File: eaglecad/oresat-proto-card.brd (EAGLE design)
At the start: 99.8 x 94.7 mm, 263 parts, among them J6 J-SAMTEC-TFM-120-X1-XXX-D-RA, Q10 DMP2240UDM, Q11 MOSFET-PCH-SOT23-6, Q12 MOSFET-PCH-SOT23-6, Q13 PMV45EN, Q14 PMV45EN, Q15 DMP2240UDM, Q16 MOSFET-PCH-SOT23-6, Q17 MOSFET-PCH-SOT23-6, Q18 PMV45EN, Q19 PMV45EN, Q20 DMP2240UDM, Q21 MOSFET-PCH-SOT23-6, Q22 MOSFET-PCH-SOT23-6, Q23 PMV45EN, Q24 PMV45EN, Q25 DMP2240UDM, Q6 MOSFET-PCH-SOT23-6, Q7 MOSFET-PCH-SOT23-6, Q8 PMV45EN, Q9 PMV45EN, U10 MAX7310ATE, U11 MAX4211CETE, U12 MCP1703A, U13 MAX7310ATE, U14 MAX4211CETE, U15 MCP1703A, U3 MAX7310ATE, U4 MAX4211CETE, U6 MCP1703A, U7 MAX7310ATE, U8 MAX4211CETE, U9 MCP1703A

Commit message: power domain updates
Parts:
- removed C21, C22: 1u, oresat-rcl:.0603-B-NOSILK
- removed C23, C24: TBD, rcl_custom:.0402-B-NOSILK
- removed C25: 100n, rcl_custom:.0402-B-NOSILK
- removed D10: AMBER, SparkFun-LED:LED-0603
- removed D9: GREEN, SparkFun-LED:LED-0603
- removed Q21, Q22: MOSFET-PCH-SOT23-6, Q-MOSFET-PCH-SOT23-6:SOT23-6
- removed Q23, Q24: PMV45EN, Tova:SOT23
- removed Q25: DMP2240UDM, Q-MOSFET-PCH-dual-SOT23-6:SOT23-6
- removed R153, R154, R163, R165, R167, R168, R38: NP, rcl_custom:.0402-B-NOSILK
- removed R155, R156, R37: 100, rcl_custom:.0402-B-NOSILK
- removed R157, R158, R159, R161, R166, R169, R171, R172, R173: 10k, rcl_custom:.0402-B-NOSILK
- removed R160: 100m, rcl:R1206
- removed R162, R164: 0, rcl_custom:.0402-B-NOSILK
- removed R170, R36: 2.7k, rcl_custom:.0402-B-NOSILK
- removed R174, R175: 47k, rcl_custom:.0402-B-NOSILK
- removed TP13, TP14, TP18, TP20, TP22: TEST-POINT, Tova:2MM-TEST-POINT
- removed U3: MAX7310ATE, U-Maxim-MAX7310-I2C-GPIO-expander:QFN65P400X400X80-17T210
- removed U4: MAX4211CETE, U-Maxim-MAX4211-power-monitor:QFN65P400X400X80-17T210
- added C6: 100n, rcl_custom:.0402-B-NOSILK
- added D11: GREEN, SparkFun-LED:LED-0603
- added D12: AMBER, SparkFun-LED:LED-0603
- added Q26, Q27: MOSFET-PCH-SOT23-6, Q-MOSFET-PCH-SOT23-6:SOT23-6
- added Q28, Q29: PMV45EN, Tova:SOT23
- added Q30: DMP2240UDM, Q-MOSFET-PCH-dual-SOT23-6:SOT23-6
- added R191, R219: 2.7k, rcl_custom:.0402-B-NOSILK
- added R192, R205, R225: 100, rcl_custom:.0402-B-NOSILK
- added R193, R194, R195, R196, R197, R198, R199, R200, R201, R202, R203, R204, R212, R214, R216, R217: NP, rcl_custom:.0402-B-NOSILK
- added R206, R207, R208, R210, R215, R218, R220, R226: 10k, rcl_custom:.0402-B-NOSILK
- added R209: 100m, rcl:R1206
- added R211, R213: 0, rcl_custom:.0402-B-NOSILK
- added R221, R222: 47k, rcl_custom:.0402-B-NOSILK
- added R223, R227: 330k, rcl_custom:.0402-B-NOSILK
- added R224, R228: 1M, rcl_custom:.0402-B-NOSILK
- added TP2, TP4, TP76, TP77, TP78, TP79, TP80, TP81, TP82, TP83, TP84, TP85, TP86, TP87, TP88, TP89, TP90: TEST-POINT, Tova:2MM-TEST-POINT
- added U16, U23, U24: MIC842LYC5, U-Microchip-MIC842-Comparator:SC70-5
- added U21, U5: MAX7310ATE, U-Maxim-MAX7310-I2C-GPIO-expander:QFN65P400X400X80-17T210
- added U22: MAX4211FETE, U-Maxim-MAX4211-power-monitor:QFN65P400X400X80-17T210
- C11: value TBD -> 100n
- C12, C17: value TBD -> NP
- C13, C19: value 100n -> 1u; device rcl_custom:.0402-B-NOSILK -> oresat-rcl:.0603-B-NOSILK
- C14, C20, C8: value NP -> 1u; device rcl_custom:.0402-B-NOSILK -> oresat-rcl:.0603-B-NOSILK
- C16: value 1u -> 100n; device oresat-rcl:.0603-B-NOSILK -> rcl_custom:.0402-B-NOSILK
- C18, C29, C30: value TBD -> 1u; device rcl_custom:.0402-B-NOSILK -> oresat-rcl:.0603-B-NOSILK
- C26: value NP -> 100n
- C27: value 1u -> NP; device oresat-rcl:.0603-B-NOSILK -> rcl_custom:.0402-B-NOSILK
- C7: value 100n -> NP
- R100, R141, R65: value 2.7k -> NP
- R102, R103, R122, R123, R124, R126, R136, R138, R52, R64, R87, R88, R89: value 10k -> NP
- R104, R139: value 47k -> 10k
- R105: value 47k -> 2.7k
- R106: value 2.7k -> 10k
- R107: value 100 -> 47k
- R108, R145, R146: value NP -> 47k
- R109, R113, R147, R151, R75: value NP -> 330k
- R110, R114, R148, R152, R76: value NP -> 1M
- R111, R116, R149, R40, R73, R78: value NP -> 100
- R112, R130, R132, R144, R150, R58, R63, R74, R93: value NP -> 10k
- R115, R143, R39, R77: value NP -> 2.7k
- R120, R121, R50, R51, R85, R86: value 100 -> NP
- R125, R90: value 100m -> NP; device rcl:R1206 -> rcl_custom:.0402-B-NOSILK
- R127: value 0 -> NP
- R129: value 0 -> 100
- R133, R95: value NP -> 100m; device rcl_custom:.0402-B-NOSILK -> rcl:R1206
- R135: value 2.7k -> 0
- R137, R61, R99: value 10k -> 0
- R140: value 47k -> NP
- R142: value 100 -> 10k
- R53, R91: value 10k -> 100
- R55: value 100m -> 10k; device rcl:R1206 -> rcl_custom:.0402-B-NOSILK
- R57: value 0 -> 100m; device rcl_custom:.0402-B-NOSILK -> rcl:R1206
- R67: value 10k -> 2.7k
- R71: value 2.7k -> 330k
- R72: value 100 -> 1M
- R92, R94: value 0 -> 10k
- R97: value NP -> 0
- U$1, U$3, U$4, U$5: value MEZZANINE_1 -> MEZZANINE_PLUG; device oresat-ACS_driver_board:MEZZANINE_1 -> oresat-ACS_driver_board:MEZZANINE_PLUG
- U10: value MAX7310ATE -> MAX4211FETE; device U-Maxim-MAX7310-I2C-GPIO-expander:QFN65P400X400X80-17T210 -> U-Maxim-MAX4211-power-monitor:QFN65P400X400X80-17T210
- U11, U8: value MAX4211CETE -> MIC842LYC5; device U-Maxim-MAX4211-power-monitor:QFN65P400X400X80-17T210 -> U-Microchip-MIC842-Comparator:SC70-5
- U12, U15: value MCP1703A -> MIC842LYC5; device v-reg:SOT23 -> U-Microchip-MIC842-Comparator:SC70-5
- U14: value MAX4211CETE -> MAX4211FETE
- U6: value MCP1703A -> MAX4211FETE; device v-reg:SOT23 -> U-Maxim-MAX4211-power-monitor:QFN65P400X400X80-17T210
- U7: value MAX7310ATE -> MIC842LYC5; device U-Maxim-MAX7310-I2C-GPIO-expander:QFN65P400X400X80-17T210 -> U-Microchip-MIC842-Comparator:SC70-5
- U9: value MCP1703A -> MAX7310ATE; device v-reg:SOT23 -> U-Maxim-MAX7310-I2C-GPIO-expander:QFN65P400X400X80-17T210
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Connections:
- removed net !SD: J6.39, J6.40, JP10.10, JP10.9
- removed net BOOT_Q1: U$3.P$22, U$3.P$9, U3.10
- removed net BOOT_Q2: U$1.P$22, U$1.P$9, U7.10
- removed net BOOT_Q3: U$4.P$22, U$4.P$9, U10.10
- removed net BOOT_Q4: U$5.P$22, U$5.P$9, U13.10
- removed net MAG1_Q1: U$3.P$10, U$3.P$21
- removed net MAG1_Q2: U$1.P$10, U$1.P$21
- removed net MAG1_Q3: U$4.P$10, U$4.P$21
- removed net MAG1_Q4: U$5.P$10, U$5.P$21
- removed net MAG2_Q1: U$3.P$11, U$3.P$20
- removed net MAG2_Q2: U$1.P$11, U$1.P$20
- removed net MAG2_Q3: U$4.P$11, U$4.P$20
- removed net MAG2_Q4: U$5.P$11, U$5.P$20
- removed net N$63: Q17.3, Q18.3, R123.1
- removed net N$64: Q17.1, Q17.2, Q17.5, Q17.6, R125.1, U11.16
- removed net N$65: R127.1, R128.2, TP39.1, U11.10
- removed net N$66: R129.1, R130.2, TP38.1, U11.11
- removed net N$67: R127.2, U11.14
- removed net N$68: R129.2, U11.12, U11.9
- removed net N$69: TP37.1, U11.13
- removed net N$70: R133.1, U11.5
- removed net N$71: C20.1, R132.2, R133.2
- removed net N$72: C21.1, Q16.4, R125.2, R131.2, U11.15, U12.3
- removed net N$73: R135.2, TP46.1, U10.12
- removed net N$74: D8.A, R135.1
- removed net N$75: C23.1, Q20.5, R121.2
- removed net N$76: C23.2, Q20.1, Q20.4, R136.2
- removed net N$77: C24.2, Q20.3, R137.2, R138.1
- removed net N$78: R139.1, R140.1, TP45.1, U10.11
- removed net N$80: D9.A, R141.1
- removed net N$81: R157.1, U13.13
- removed net SCL_Q1: R70.2, U$3.P$24, U$3.P$7, U3.8
- removed net SCL_Q2: R105.2, U$1.P$24, U$1.P$7, U7.8
- removed net SCL_Q3: R140.2, U$4.P$24, U$4.P$7, U10.8
- removed net SCL_Q4: R175.2, U$5.P$24, U$5.P$7, U13.8
- removed net SDA_Q1: R69.2, U$3.P$23, U$3.P$8, U3.9
- removed net SDA_Q2: R104.2, U$1.P$23, U$1.P$8, U7.9
- removed net SDA_Q3: R139.2, U$4.P$23, U$4.P$8, U10.9
- removed net SDA_Q4: R174.2, U$5.P$23, U$5.P$8, U13.9
- new net BOOT0_Q1: U5.10
- new net BOOT0_Q2: U13.10
- new net BOOT0_Q3: U9.10
- new net BOOT0_Q4: U21.10
- new net IOUT1: R59.2, U6.14
- new net IOUT2: R135.2, U14.14
- new net IOUT3: R97.2, U10.14
- new net IOUT4: R211.2, U22.14
- new net N$10: R61.1, R62.2, TP4.1, U6.11
- new net N$100: C29.1, R223.1, R224.1, U24.1
- new net N$11: R61.2, U6.12, U6.8
- new net N$12: R65.1, U6.5
- new net N$13: C7.1, R64.2, R65.2
- new net N$14: Q6.4, R57.2, R63.2, U6.15
- new net N$15: D4.A, R67.1
- new net N$16: Q10.5, R53.2
- new net N$17: Q10.1, R68.2, TP29.1, U8.4
- new net N$18: R69.1, R70.1, TP28.1, U5.11
- new net N$19: Q10.2, R73.2
- new net N$20: Q10.3, R74.2, TP30.1, U7.4
- new net N$5: D3.A, R39.1
- new net N$6: R54.1, U5.13
- new net N$7: Q7.3, Q8.3, R55.1
- new net N$8: Q7.1, Q7.2, Q7.5, Q7.6, R57.1, U6.16
- new net N$9: R59.1, R60.2, TP15.1, U6.10
- new net N$99: C30.1, R227.1, R228.1, U23.1
- new net PB6/SCL_Q1: R70.2, U5.4
- new net PB6/SCL_Q2: R146.2, U13.4
- new net PB6/SCL_Q3: R108.2, U9.4
- new net PB6/SCL_Q4: R222.2, U21.4
- new net PB7/SDA_Q1: R69.2, U5.5
- new net PB7/SDA_Q2: R145.2, U13.5
- new net PB7/SDA_Q3: R107.2, U9.5
- new net PB7/SDA_Q4: R221.2, U21.5
- new net POUT_Q1: TP2.1, U6.13
- new net POUT_Q2: TP46.1, U14.13
- new net POUT_Q3: TP31.1, U10.13
- new net POUT_Q4: TP76.1, U22.13
- net !FAULT_Q1: now also R66.1, TP19.1, U5.7; no longer R64.1, TP18.1, U3.7
- net !FAULT_Q2: now also Q19.3, R142.1, TP51.1, U13.7; no longer Q14.3, R99.1, TP30.1, U7.7
- net !FAULT_Q3: now also Q14.3, R104.1, TP36.1, U9.7; no longer Q19.3, R134.1, TP42.1, U10.7
- net !FAULT_Q4: now also Q29.3, R218.1, TP81.1, U21.7; no longer Q24.3, R169.1, TP54.1, U13.7
- net AD0_Q1: now also R42.2, R43.2, R44.1, U5.1; no longer R38.1, R39.2, R40.2, U3.1
- net AD0_Q2: now also R117.1, R118.2, R119.2, R120.1, U13.1; no longer R73.1, R74.2, R75.2, R76.1, U7.1
- net AD0_Q3: now also R79.1, R80.2, R81.2, R82.1, U9.1; no longer R108.1, R109.2, R110.2, R111.1, U10.1
- net AD0_Q4: now also R193.1, R194.2, R195.2, R196.1, U21.1; no longer R143.1, R144.2, R145.2, R146.1, U13.1
- net AD1_Q1: now also R46.2, R47.2, R48.1, U5.2; no longer R42.1, R43.2, R44.2, U3.2
- net AD1_Q2: now also R121.1, R122.2, R123.2, R124.1, U13.2; no longer R77.1, R78.2, R79.2, R80.1, U7.2
- net AD1_Q3: now also R83.1, R84.2, R85.2, R86.1, U9.2; no longer R112.1, R113.2, R114.2, R115.1, U10.2
- net AD1_Q4: now also R197.1, R198.2, R199.2, R200.1, U21.2; no longer R147.1, R148.2, R149.2, R150.1, U13.2
- net AD2_Q1: now also R50.2, R51.2, R52.1, U5.3; no longer R46.1, R47.2, R48.2, U3.3
- net AD2_Q2: now also R125.1, R126.2, R127.2, R128.1, U13.3; no longer R81.1, R82.2, R83.2, R84.1, U7.3
- net AD2_Q3: now also R87.1, R88.2, R89.2, R90.1, U9.3; no longer R116.1, R117.2, R118.2, R119.1, U10.3
- net AD2_Q4: now also R201.1, R202.2, R203.2, R204.1, U21.3; no longer R151.1, R152.2, R153.2, R154.1, U13.3
- net CAN2_H: no longer U$1.P$25, U$1.P$6, U$3.P$25, U$3.P$6, U$4.P$25, U$4.P$6, U$5.P$25, U$5.P$6
- net CAN2_L: no longer U$1.P$26, U$1.P$5, U$3.P$26, U$3.P$5, U$4.P$26, U$4.P$5, U$5.P$26, U$5.P$5
- net CB-RESET_Q1: now also R58.2, U5.9, U6.9; no longer R56.2, U3.5, U4.8
- net CB-RESET_Q2: now also R134.2, TP50.1, U13.9, U14.9; no longer R91.2, TP29.1, U7.5, U8.8
- net CB-RESET_Q3: now also R96.2, TP35.1, U10.9, U9.9; no longer R126.2, TP41.1, U10.5, U11.8
- net CB-RESET_Q4: now also R210.2, TP80.1, U21.9, U22.9; no longer R161.2, TP53.1, U13.5, U14.8
- net CB_CTRL_Q1: now also R63.1, TP27.1, U6.3, U6.4, U6.6; no longer R61.1, U4.3, U4.4, U4.6
- net CB_CTRL_Q2: now also Q16.3, Q19.1, R139.1, TP57.1, U14.3, U14.4, U14.6; no longer Q11.3, Q14.1, R96.1, U8.3, U8.4, U8.6
- net CB_CTRL_Q3: now also Q11.3, Q14.1, R101.1, TP42.1, U10.3, U10.4, U10.6; no longer Q16.3, Q19.1, R131.1, U11.3, U11.4, U11.6
- net CB_CTRL_Q4: now also Q26.3, Q29.1, R215.1, TP87.1, U22.3, U22.4, U22.6; no longer Q21.3, Q24.1, R166.1, U14.3, U14.4, U14.6
- net GND: now also C11.1, C13.2, C14.2, C16.1, C18.2, C19.2, C20.2, C26.1, C29.2, C30.2, C6.1, C8.2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; no longer C13.1, C16.2, C19.1, C21.2, C22.2, C25.1, C27.2, C7.1, D10.C, D9.C, Q23.2, Q24.2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
- net MAX4211-3V3_Q1: now also C8.1, TP24.1, U5.12, U6.1; no longer C10.1, U4.1, U6.2
- net MAX4211-3V3_Q2: now also C18.1, TP54.1, U13.12, U14.1; no longer C16.1, U8.1, U9.2
- net MAX4211-3V3_Q3: now also C13.1, TP39.1, U10.1, U9.12; no longer C22.1, U11.1, U12.2
- net MAX4211-3V3_Q4: now also TP84.1, U21.12, U22.1; no longer U14.1, U15.2
- net N$21: now also C10.1, R75.1, R76.1, U7.1; no longer D3.A, R36.1
- net N$22: now also C9.1, R71.1, R72.1, U8.1; no longer R52.1, U3.13
- net N$23: now also D5.A, R77.1; no longer Q7.3, Q8.3, R53.1
- net N$24: now also R92.1, U9.13; no longer Q7.1, Q7.2, Q7.5, Q7.6, R55.1, U4.16
- net N$25: now also Q12.3, Q13.3, R93.1; no longer R57.1, R58.2, TP15.1, U4.10
- net N$26: now also Q12.1, Q12.2, Q12.5, Q12.6, R95.1, U10.16; no longer R59.1, R60.2, TP14.1, U4.11
- net N$27: now also R97.1, R98.2, TP33.1, U10.10; no longer R57.2, U4.14
- net N$28: now also R100.2, R99.1, TP32.1, U10.11; no longer R59.2, U4.12, U4.9
- net N$29: now also R99.2, U10.12, U10.8; no longer TP13.1, U4.13
- net N$30: now also R103.1, U10.5; no longer R63.1, U4.5
- net N$31: now also C12.1, R102.2, R103.2; no longer C8.1, R62.2, R63.2
- net N$32: now also Q11.4, R101.2, R95.2, U10.15; no longer C9.1, Q6.4, R55.2, R61.2, U4.15, U6.3
- net N$33: now also D6.A, R105.1; no longer R65.2, TP22.1, U3.12
- net N$34: now also Q15.5, R91.2; no longer D4.A, R65.1
- net N$35: now also Q15.1, R106.2, TP44.1, U12.4; no longer C11.1, Q10.5, R51.2
- net N$36: now also R107.1, R108.1, TP43.1, U9.11; no longer C11.2, Q10.1, Q10.4, R66.2
- net N$37: now also Q15.2, R111.2; no longer C12.2, Q10.3, R67.2, R68.1
- net N$38: now also Q15.3, R112.2, TP45.1, U11.4; no longer R69.1, R70.1, TP21.1, U3.11
- net N$41: now also C15.1, R113.1, R114.1, U11.1; no longer D5.A, R71.1
- net N$42: now also C14.1, R109.1, R110.1, U12.1; no longer R87.1, U7.13
- net N$43: now also D7.A, R115.1; no longer Q12.3, Q13.3, R88.1
- net N$44: now also R130.1, U13.13; no longer Q12.1, Q12.2, Q12.5, Q12.6, R90.1, U8.16
- net N$45: now also Q17.3, Q18.3, R131.1; no longer R92.1, R93.2, TP27.1, U8.10
- net N$46: now also Q17.1, Q17.2, Q17.5, Q17.6, R133.1, U14.16; no longer R94.1, R95.2, TP26.1, U8.11
- net N$47: now also R135.1, R136.2, TP48.1, U14.10; no longer R92.2, U8.14
- net N$48: now also R137.1, R138.2, TP47.1, U14.11; no longer R94.2, U8.12, U8.9
- net N$49: now also R137.2, U14.12, U14.8; no longer TP25.1, U8.13
- net N$50: now also R141.1, U14.5; no longer R98.1, U8.5
- net N$51: now also C17.1, R140.2, R141.2; no longer C14.1, R97.2, R98.2
- net N$52: now also Q16.4, R133.2, R139.2, U14.15; no longer C15.1, Q11.4, R90.2, R96.2, U8.15, U9.3
- net N$53: now also D8.A, R143.1; no longer R100.2, TP34.1, U7.12
- net N$54: now also Q20.5, R129.2; no longer D6.A, R100.1
- net N$55: now also Q20.1, R144.2, TP59.1, U16.4; no longer C17.1, Q15.5, R86.2
- net N$56: now also R145.1, R146.1, TP58.1, U13.11; no longer C17.2, Q15.1, Q15.4, R101.2
- net N$58: now also Q20.2, R149.2; no longer C18.2, Q15.3, R102.2, R103.1
- net N$59: now also Q20.3, R150.2, TP60.1, U15.4; no longer R104.1, R105.1, TP33.1, U7.11
- net N$61: now also C20.1, R151.1, R152.1, U15.1; no longer D7.A, R106.1
- net N$62: now also C19.1, R147.1, R148.1, U16.1; no longer R122.1, U10.13
- net N$82: now also D11.A, R191.1; no longer Q22.3, Q23.3, R158.1
- net N$83: now also R206.1, U21.13; no longer Q22.1, Q22.2, Q22.5, Q22.6, R160.1, U14.16
- net N$84: now also Q27.3, Q28.3, R207.1; no longer R162.1, R163.2, TP51.1, U14.10
- net N$85: now also Q27.1, Q27.2, Q27.5, Q27.6, R209.1, U22.16; no longer R164.1, R165.2, TP50.1, U14.11
- net N$86: now also R211.1, R212.2, TP78.1, U22.10; no longer R162.2, U14.14
- net N$87: now also R213.1, R214.2, TP77.1, U22.11; no longer R164.2, U14.12, U14.9
- net N$88: now also R213.2, U22.12, U22.8; no longer TP49.1, U14.13
- net N$89: now also R217.1, U22.5; no longer R168.1, U14.5
- net N$90: now also C27.1, R216.2, R217.2; no longer C26.1, R167.2, R168.2
- net N$91: now also Q26.4, R209.2, R215.2, U22.15; no longer C27.1, Q21.4, R160.2, R166.2, U14.15, U15.3
- net N$92: now also D12.A, R219.1; no longer R170.2, TP58.1, U13.12
- net N$93: now also Q30.5, R205.2; no longer D10.A, R170.1
- net N$94: now also Q30.1, R220.2, TP89.1, U24.4; no longer C29.1, Q25.5, R156.2
- net N$95: now also R221.1, R222.1, TP88.1, U21.11; no longer C29.2, Q25.1, Q25.4, R171.2
- net N$96: now also Q30.2, R225.2; no longer C30.2, Q25.3, R172.2, R173.1
- net N$97: now also Q30.3, R226.2, TP90.1, U23.4; no longer R174.1, R175.1, TP57.1, U13.11
- net ON/!OFF_Q1: now also R56.2, R67.2, U5.8; no longer R54.2, U3.4
- net ON/!OFF_Q2: now also Q18.1, R132.2, R143.2, TP49.1, U13.8; no longer Q13.1, R89.2, TP28.1, U7.4
- net ON/!OFF_Q3: now also Q13.1, R105.2, R94.2, TP34.1, U9.8; no longer Q18.1, R124.2, TP40.1, U10.4
- net ON/!OFF_Q4: now also Q28.1, R208.2, R219.2, TP79.1, U21.8; no longer Q23.1, R159.2, TP52.1, U13.4
- net OPD_PWR: now also R116.1, R192.1, R40.1, R78.1; no longer R107.1, R142.1, R37.1, R72.1
- net OPD_SCL: now also R111.1, R149.1, R225.1, R73.1; no longer R120.1, R155.1, R50.1, R85.1
- net OPD_SDA: now also R129.1, R205.1, R53.1, R91.1; no longer R121.1, R156.1, R51.1, R86.1
- net PEN-SCL-FILT_Q1: now also Q10.4, R42.1, R46.1, R50.1, R75.2, TP25.1, U5.15; no longer R39.1, R43.1, R47.1, R50.2, TP23.1, U3.15
- net PEN-SCL-FILT_Q2: now also Q20.4, R118.1, R122.1, R126.1, R151.2, TP55.1, U13.15; no longer R74.1, R78.1, R82.1, R85.2, TP35.1, U7.15
- net PEN-SCL-FILT_Q3: now also Q15.4, R113.2, R80.1, R84.1, R88.1, TP40.1, U9.15; no longer R109.1, R113.1, R117.1, R120.2, TP47.1, U10.15
- net PEN-SCL-FILT_Q4: now also Q30.4, R194.1, R198.1, R202.1, R227.2, TP85.1, U21.15; no longer R144.1, R148.1, R152.1, R155.2, TP59.1, U13.15
- net PEN-SDA-FILT_Q1: now also R44.2, R48.2, R52.2, R71.2, TP26.1, U5.16; no longer R41.2, R45.2, R49.2, R67.1, TP24.1, U3.16
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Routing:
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- removed copper zone on layer 16, net N$24
- removed copper zone on layer 16, net N$44
- removed copper zone on layer 16, net N$64
- removed copper zone on layer 16, net N$83
- removed copper zone on layer 16, net VBUSP_Q1
- removed copper zone on layer 16, net VBUSP_Q2
- removed copper zone on layer 16, net VBUSP_Q3
- removed copper zone on layer 16, net VBUSP_Q4

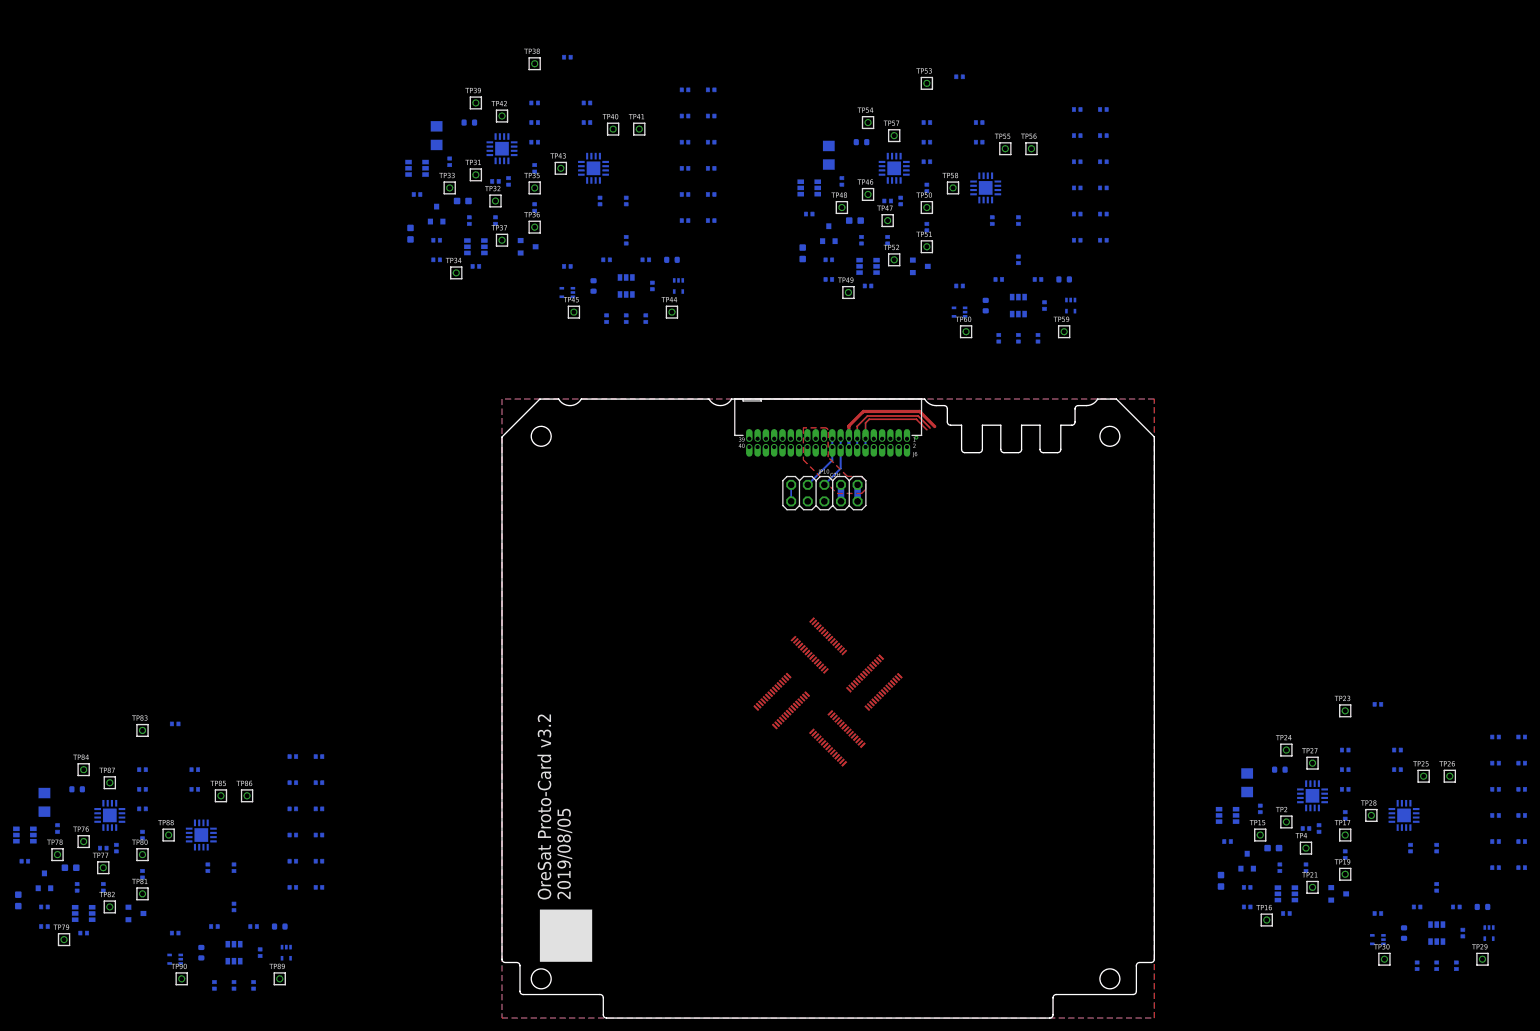
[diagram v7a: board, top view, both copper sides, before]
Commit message: ACS power domaine routing in progress
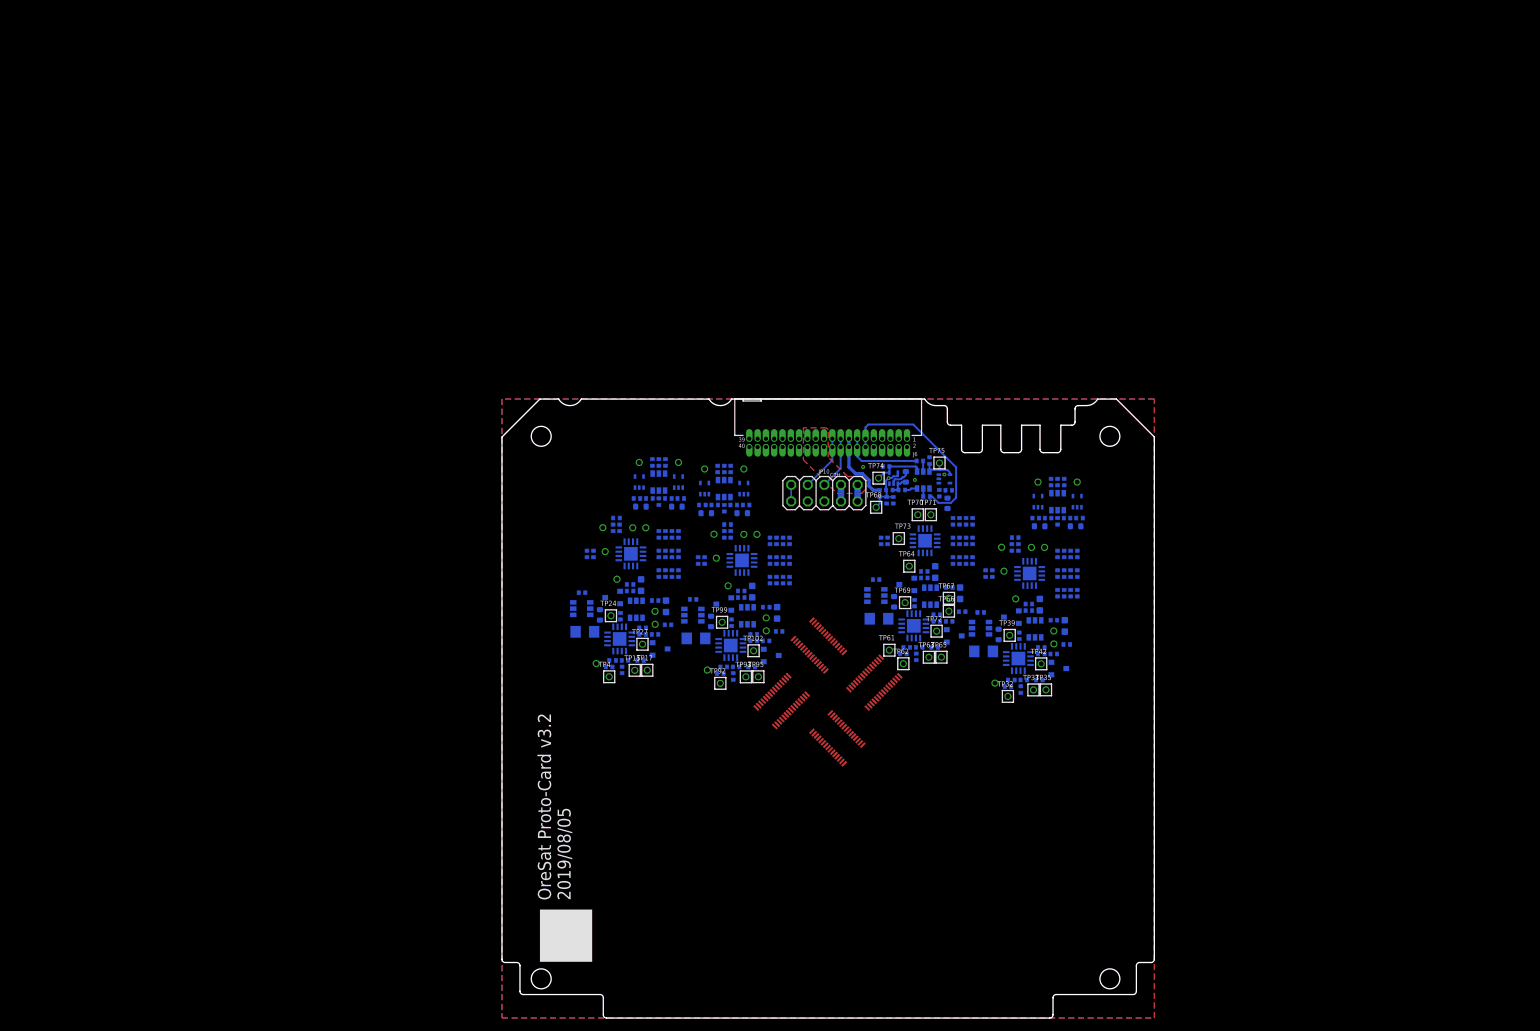
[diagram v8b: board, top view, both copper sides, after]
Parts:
- removed C16, C26: 100n, rcl_custom:.0402-B-NOSILK
- removed C17, C27, R117, R118, R119, R120, R121, R122, R123, R124, R125, R126, R127, R128, R136, R138, R140, R141, R193, R194, R195, R196, R197, R198, R199, R200, R201, R202, R203, R204, R212, R214, R216, R217: NP, rcl_custom:.0402-B-NOSILK
- removed C18, C19, C20, C28, C29, C30: 1u, oresat-rcl:.0603-B-NOSILK
- removed D11, D7: GREEN, SparkFun-LED:LED-0603
- removed D12, D8: AMBER, SparkFun-LED:LED-0603
- removed Q16, Q17, Q26, Q27: MOSFET-PCH-SOT23-6, Q-MOSFET-PCH-SOT23-6:SOT23-6
- removed Q18, Q19, Q28, Q29: PMV45EN, Tova:SOT23
- removed Q20, Q30: DMP2240UDM, Q-MOSFET-PCH-dual-SOT23-6:SOT23-6
- removed R115, R143, R191, R219: 2.7k, rcl_custom:.0402-B-NOSILK
- removed R116, R129, R149, R192, R205, R225: 100, rcl_custom:.0402-B-NOSILK
- removed R130, R131, R132, R134, R139, R142, R144, R150, R206, R207, R208, R210, R215, R218, R220, R226: 10k, rcl_custom:.0402-B-NOSILK
- removed R133, R209: 100m, rcl:R1206
- removed R135, R137, R211, R213: 0, rcl_custom:.0402-B-NOSILK
- removed R145, R146, R221, R222: 47k, rcl_custom:.0402-B-NOSILK
- removed R147, R151, R223, R227: 330k, rcl_custom:.0402-B-NOSILK
- removed R148, R152, R224, R228: 1M, rcl_custom:.0402-B-NOSILK
- removed TP46, TP47, TP48, TP49, TP50, TP51, TP52, TP53, TP54, TP55, TP56, TP57, TP58, TP59, TP60, TP76, TP77, TP78, TP79, TP80, TP81, TP82, TP83, TP84, TP85, TP86, TP87, TP88, TP89, TP90: TEST-POINT, Tova:2MM-TEST-POINT
- removed U13, U21: MAX7310ATE, U-Maxim-MAX7310-I2C-GPIO-expander:QFN65P400X400X80-17T210
- removed U14, U22: MAX4211FETE, U-Maxim-MAX4211-power-monitor:QFN65P400X400X80-17T210
- removed U15, U16, U23, U24: MIC842LYC5, U-Microchip-MIC842-Comparator:SC70-5
- added C21, C31: 100n, rcl_custom:.0402-B-NOSILK
- added C22, C32, R155, R156, R157, R158, R159, R160, R161, R162, R163, R164, R165, R166, R174, R176, R178, R179, R231, R232, R233, R234, R235, R236, R237, R238, R239, R240, R241, R242, R250, R252, R254, R255: NP, rcl_custom:.0402-B-NOSILK
- added C23, C24, C25, C33, C34, C35: 1u, oresat-rcl:.0603-B-NOSILK
- added D10, D14: AMBER, SparkFun-LED:LED-0603
- added D13, D9: GREEN, SparkFun-LED:LED-0603
- added Q21, Q22, Q31, Q32: MOSFET-PCH-SOT23-6, Q-MOSFET-PCH-SOT23-6:SOT23-6
- added Q23, Q24, Q33, Q34: PMV45EN, Tova:SOT23
- added Q25, Q35: DMP2240UDM, Q-MOSFET-PCH-dual-SOT23-6:SOT23-6
- added R153, R181, R229, R257: 2.7k, rcl_custom:.0402-B-NOSILK
- added R154, R167, R187, R230, R243, R263: 100, rcl_custom:.0402-B-NOSILK
- added R168, R169, R170, R172, R177, R180, R182, R188, R244, R245, R246, R248, R253, R256, R258, R264: 10k, rcl_custom:.0402-B-NOSILK
- added R171, R247: 100m, rcl:R1206
- added R173, R175, R249, R251: 0, rcl_custom:.0402-B-NOSILK
- added R183, R184, R259, R260: 47k, rcl_custom:.0402-B-NOSILK
- added R185, R189, R261, R265: 330k, rcl_custom:.0402-B-NOSILK
- added R186, R190, R262, R266: 1M, rcl_custom:.0402-B-NOSILK
- added TP100, TP101, TP102, TP103, TP104, TP105, TP61, TP62, TP63, TP64, TP65, TP66, TP67, TP68, TP69, TP70, TP71, TP72, TP73, TP74, TP75, TP91, TP92, TP93, TP94, TP95, TP96, TP97, TP98, TP99: TEST-POINT, Tova:2MM-TEST-POINT
- added U17, U25: MAX7310ATE, U-Maxim-MAX7310-I2C-GPIO-expander:QFN65P400X400X80-17T210
- added U18, U26: MAX4211FETE, U-Maxim-MAX4211-power-monitor:QFN65P400X400X80-17T210
- added U19, U20, U27, U28: MIC842LYC5, U-Microchip-MIC842-Comparator:SC70-5
- moved TP29 149.7 mm to (21.0, 85.0), flipped to the bottom, turned to 270 degrees
- moved U8 147.2 mm to (21.0, 82.0), turned to 0 degrees
- moved R68 145.1 mm to (23.0, 85.0), turned to 270 degrees
- moved R72 142.8 mm to (20.6, 79.5), turned to 0 degrees
- moved C9 142.6 mm to (21.2, 78.2), turned to 0 degrees
- moved R73 141.7 mm to (24.0, 85.0), turned to 270 degrees
- moved R50 138.5 mm to (25.0, 68.0), turned to 270 degrees
- moved R74 138.4 mm to (25.0, 85.0), turned to 270 degrees
- moved R71 138.4 mm to (22.6, 79.5), turned to 180 degrees
- moved R52 138.2 mm to (24.0, 68.0), turned to 90 degrees
- moved Q10 137.6 mm to (24.0, 82.0), turned to 180 degrees
- moved R46 137.0 mm to (25.0, 71.0), turned to 270 degrees
- moved R48 136.8 mm to (24.0, 71.0), turned to 90 degrees
- moved R70 136.6 mm to (14.0, 71.0), turned to 270 degrees
- moved R42 135.6 mm to (25.0, 74.0), turned to 270 degrees
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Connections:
- net IOUT1 renamed IOUT_Q4
- net IOUT3 renamed IOUT_Q1
- removed net IOUT2: R135.2, U14.14
- removed net IOUT4: R211.2, U22.14
- removed net N$100: C29.1, R223.1, R224.1, U24.1
- removed net N$43: D7.A, R115.1
- removed net N$44: R130.1, U13.13
- removed net N$45: Q17.3, Q18.3, R131.1
- removed net N$46: Q17.1, Q17.2, Q17.5, Q17.6, R133.1, U14.16
- removed net N$47: R135.1, R136.2, TP48.1, U14.10
- removed net N$48: R137.1, R138.2, TP47.1, U14.11
- removed net N$49: R137.2, U14.12, U14.8
- removed net N$50: R141.1, U14.5
- removed net N$51: C17.1, R140.2, R141.2
- removed net N$52: Q16.4, R133.2, R139.2, U14.15
- removed net N$53: D8.A, R143.1
- removed net N$54: Q20.5, R129.2
- removed net N$55: Q20.1, R144.2, TP59.1, U16.4
- removed net N$56: R145.1, R146.1, TP58.1, U13.11
- removed net N$58: Q20.2, R149.2
- removed net N$59: Q20.3, R150.2, TP60.1, U15.4
- removed net N$61: C20.1, R151.1, R152.1, U15.1
- removed net N$62: C19.1, R147.1, R148.1, U16.1
- removed net N$82: D11.A, R191.1
- removed net N$83: R206.1, U21.13
- removed net N$84: Q27.3, Q28.3, R207.1
- removed net N$85: Q27.1, Q27.2, Q27.5, Q27.6, R209.1, U22.16
- removed net N$86: R211.1, R212.2, TP78.1, U22.10
- removed net N$87: R213.1, R214.2, TP77.1, U22.11
- removed net N$88: R213.2, U22.12, U22.8
- removed net N$89: R217.1, U22.5
- removed net N$90: C27.1, R216.2, R217.2
- removed net N$91: Q26.4, R209.2, R215.2, U22.15
- removed net N$92: D12.A, R219.1
- removed net N$93: Q30.5, R205.2
- removed net N$94: Q30.1, R220.2, TP89.1, U24.4
- removed net N$95: R221.1, R222.1, TP88.1, U21.11
- removed net N$96: Q30.2, R225.2
- removed net N$97: Q30.3, R226.2, TP90.1, U23.4
- removed net N$99: C30.1, R227.1, R228.1, U23.1
- new net IOUT_Q2: R173.2, U18.14
- new net IOUT_Q_3: R249.2, U26.14
- new net MAG1_Q1: U$1.P$10, U$1.P$21
- new net MAG1_Q2: U$3.P$10, U$3.P$21
- new net MAG1_Q3: U$4.P$10, U$4.P$21
- new net MAG1_Q4: U$5.P$10, U$5.P$21
- new net MAG2_Q1: U$1.P$11, U$1.P$20
- new net MAG2_Q2: U$3.P$11, U$3.P$20
- new net MAG2_Q3: U$4.P$11, U$4.P$20
- new net MAG2_Q4: U$5.P$11, U$5.P$20
- new net N$205: D9.A, R153.1
- new net N$206: R168.1, U17.13
- new net N$207: Q22.3, Q23.3, R169.1
- new net N$208: Q22.1, Q22.2, Q22.5, Q22.6, R171.1, U18.16
- new net N$209: R173.1, R174.2, TP63.1, U18.10
- new net N$210: R175.1, R176.2, TP62.1, U18.11
- new net N$211: R175.2, U18.12, U18.8
- new net N$212: R179.1, U18.5
- new net N$213: C22.1, R178.2, R179.2
- new net N$214: Q21.4, R171.2, R177.2, U18.15
- new net N$215: D10.A, R181.1
- new net N$216: Q25.5, R167.2
- new net N$217: Q25.1, R182.2, TP74.1, U20.4
- new net N$218: R183.1, R184.1, TP73.1, U17.11
- new net N$219: Q25.2, R187.2
- new net N$220: Q25.3, R188.2, TP75.1, U19.4
- new net N$221: C25.1, R189.1, R190.1, U19.1
- new net N$222: C24.1, R185.1, R186.1, U20.1
- new net N$241: D13.A, R229.1
- new net N$242: R244.1, U25.13
- new net N$243: Q32.3, Q33.3, R245.1
- new net N$244: Q32.1, Q32.2, Q32.5, Q32.6, R247.1, U26.16
- new net N$245: R249.1, R250.2, TP93.1, U26.10
- new net N$246: R251.1, R252.2, TP92.1, U26.11
- new net N$247: R251.2, U26.12, U26.8
- new net N$248: R255.1, U26.5
- new net N$249: C32.1, R254.2, R255.2
- new net N$250: Q31.4, R247.2, R253.2, U26.15
- new net N$251: D14.A, R257.1
- new net N$252: Q35.5, R243.2
- new net N$253: Q35.1, R258.2, TP104.1, U28.4
- new net N$254: R259.1, R260.1, TP103.1, U25.11
- new net N$255: Q35.2, R263.2
- new net N$256: Q35.3, R264.2, TP105.1, U27.4
- new net N$257: C35.1, R265.1, R266.1, U27.1
- new net N$258: C34.1, R261.1, R262.1, U28.1
- net !FAULT_Q1: now also Q14.3, R104.1, TP36.1, U9.7; no longer Q9.3, R66.1, TP19.1, U5.7
- net !FAULT_Q2: now also Q24.3, R180.1, TP66.1, U17.7; no longer Q19.3, R142.1, TP51.1, U13.7
- net !FAULT_Q3: now also Q34.3, R256.1, TP96.1, U25.7; no longer Q14.3, R104.1, TP36.1, U9.7
- net !FAULT_Q4: now also Q9.3, R66.1, TP19.1, U5.7; no longer Q29.3, R218.1, TP81.1, U21.7
- net AD0_Q1: now also R79.1, R80.2, R81.2, R82.1, U9.1; no longer R41.1, R42.2, R43.2, R44.1, U5.1
- net AD0_Q2: now also R155.1, R156.2, R157.2, R158.1, U17.1; no longer R117.1, R118.2, R119.2, R120.1, U13.1
- net AD0_Q3: now also R231.1, R232.2, R233.2, R234.1, U25.1; no longer R79.1, R80.2, R81.2, R82.1, U9.1
- net AD0_Q4: now also R41.1, R42.2, R43.2, R44.1, U5.1; no longer R193.1, R194.2, R195.2, R196.1, U21.1
- net AD1_Q1: now also R83.1, R84.2, R85.2, R86.1, U9.2; no longer R45.1, R46.2, R47.2, R48.1, U5.2
- net AD1_Q2: now also R159.1, R160.2, R161.2, R162.1, U17.2; no longer R121.1, R122.2, R123.2, R124.1, U13.2
- net AD1_Q3: now also R235.1, R236.2, R237.2, R238.1, U25.2; no longer R83.1, R84.2, R85.2, R86.1, U9.2
- net AD1_Q4: now also R45.1, R46.2, R47.2, R48.1, U5.2; no longer R197.1, R198.2, R199.2, R200.1, U21.2
- net AD2_Q1: now also R87.1, R88.2, R89.2, R90.1, U9.3; no longer R49.1, R50.2, R51.2, R52.1, U5.3
- net AD2_Q2: now also R163.1, R164.2, R165.2, R166.1, U17.3; no longer R125.1, R126.2, R127.2, R128.1, U13.3
- net AD2_Q3: now also R239.1, R240.2, R241.2, R242.1, U25.3; no longer R87.1, R88.2, R89.2, R90.1, U9.3
- net AD2_Q4: now also R49.1, R50.2, R51.2, R52.1, U5.3; no longer R201.1, R202.2, R203.2, R204.1, U21.3
- net BOOT0_Q1: now also U$1.P$22, U$1.P$9, U9.10; no longer U5.10
- net BOOT0_Q2: now also U$3.P$22, U$3.P$9, U17.10; no longer U13.10
- net BOOT0_Q3: now also U$4.P$22, U$4.P$9, U25.10; no longer U9.10
- net BOOT0_Q4: now also U$5.P$22, U$5.P$9, U5.10; no longer U21.10
- net CAN2_H: now also U$1.P$25, U$1.P$6, U$3.P$25, U$3.P$6, U$4.P$25, U$4.P$6, U$5.P$25, U$5.P$6
- net CAN2_L: now also U$1.P$26, U$1.P$5, U$3.P$26, U$3.P$5, U$4.P$26, U$4.P$5, U$5.P$26, U$5.P$5
- net CB-RESET_Q1: now also R96.2, TP35.1, U10.9, U9.9; no longer R58.2, TP17.1, U5.9, U6.9
- net CB-RESET_Q2: now also R172.2, TP65.1, U17.9, U18.9; no longer R134.2, TP50.1, U13.9, U14.9
- net CB-RESET_Q3: now also R248.2, TP95.1, U25.9, U26.9; no longer R96.2, TP35.1, U10.9, U9.9
- net CB-RESET_Q4: now also R58.2, TP17.1, U5.9, U6.9; no longer R210.2, TP80.1, U21.9, U22.9
- net CB_CTRL_Q1: now also Q11.3, Q14.1, R101.1, TP42.1, U10.3, U10.4, U10.6; no longer Q6.3, Q9.1, R63.1, TP27.1, U6.3, U6.4, U6.6
- net CB_CTRL_Q2: now also Q21.3, Q24.1, R177.1, TP72.1, U18.3, U18.4, U18.6; no longer Q16.3, Q19.1, R139.1, TP57.1, U14.3, U14.4, U14.6
- net CB_CTRL_Q3: now also Q31.3, Q34.1, R253.1, TP102.1, U26.3, U26.4, U26.6; no longer Q11.3, Q14.1, R101.1, TP42.1, U10.3, U10.4, U10.6
- net CB_CTRL_Q4: now also Q6.3, Q9.1, R63.1, TP27.1, U6.3, U6.4, U6.6; no longer Q26.3, Q29.1, R215.1, TP87.1, U22.3, U22.4, U22.6
- net GND: now also C21.1, C23.2, C24.2, C25.2, C31.1, C33.2, C34.2, C35.2, D10.C, D13.C, D14.C, D9.C, Q23.2, Q24.2, Q33.2, Q34.2, R157.1, R161.1, R165.1, R170.1, R172.1, R174.1, R176.1, R178.1, R182.1, R188.1, R233.1, R237.1, R241.1, R246.1, R248.1, R250.1, R252.1, R254.1, R258.1, R264.1, U$1.P$1, U$1.P$14, U$1.P$15, U$1.P$16, U$1.P$17, U$1.P$2, U$1.P$29, U$1.P$30, U$3.P$1, U$3.P$14, U$3.P$15, U$3.P$16, U$3.P$17, U$3.P$2, U$3.P$29, U$3.P$30, U$4.P$1, U$4.P$14, U$4.P$15, U$4.P$16, U$4.P$17, U$4.P$2, U$4.P$29, U$4.P$30, U$5.P$1, U$5.P$14, U$5.P$15, U$5.P$16, U$5.P$17, U$5.P$2, U$5.P$29, U$5.P$30, U17.6, U17.EPAD, U18.7, U18.EPAD, U19.2, U20.2, U25.6, U25.EPAD, U26.7, U26.EPAD, U27.2, U28.2; no longer C16.1, C18.2, C19.2, C20.2, C26.1, C28.2, C29.2, C30.2, D11.C, D12.C, D7.C, D8.C, Q18.2, Q19.2, Q28.2, Q29.2, R119.1, R123.1, R127.1, R132.1, R134.1, R136.1, R138.1, R140.1, R144.1, R150.1, R195.1, R199.1, R203.1, R208.1, R210.1, R212.1, R214.1, R216.1, R220.1, R226.1, U13.6, U13.EPAD, U14.7, U14.EPAD, U15.2, U16.2, U21.6, U21.EPAD, U22.7, U22.EPAD, U23.2, U24.2
- net MAX4211-3V3_Q1: now also C13.1, TP39.1, U10.1, U9.12; no longer C8.1, TP24.1, U5.12, U6.1
- net MAX4211-3V3_Q2: now also C23.1, TP69.1, U17.12, U18.1; no longer C18.1, TP54.1, U13.12, U14.1
- net MAX4211-3V3_Q3: now also C33.1, TP99.1, U25.12, U26.1; no longer C13.1, TP39.1, U10.1, U9.12
- net MAX4211-3V3_Q4: now also C8.1, TP24.1, U5.12, U6.1; no longer C28.1, TP84.1, U21.12, U22.1
- net ON/!OFF_Q1: now also Q13.1, R105.2, R94.2, TP34.1, U9.8; no longer Q8.1, R56.2, R67.2, TP16.1, U5.8
- net ON/!OFF_Q2: now also Q23.1, R170.2, R181.2, TP64.1, U17.8; no longer Q18.1, R132.2, R143.2, TP49.1, U13.8
- net ON/!OFF_Q3: now also Q33.1, R246.2, R257.2, TP94.1, U25.8; no longer Q13.1, R105.2, R94.2, TP34.1, U9.8
- net ON/!OFF_Q4: now also Q8.1, R56.2, R67.2, TP16.1, U5.8; no longer Q28.1, R208.2, R219.2, TP79.1, U21.8
- net OPD_PWR: now also R154.1, R230.1; no longer R116.1, R192.1
- net OPD_SCL: now also R187.1, R263.1; no longer R149.1, R225.1
- net OPD_SDA: now also R167.1, R243.1; no longer R129.1, R205.1
- net PB6/SCL_Q1: now also R108.2, U$1.P$24, U$1.P$7, U9.4; no longer R70.2, U5.4
- net PB6/SCL_Q2: now also R184.2, U$3.P$24, U$3.P$7, U17.4; no longer R146.2, U13.4
- net PB6/SCL_Q3: now also R260.2, U$4.P$24, U$4.P$7, U25.4; no longer R108.2, U9.4
- net PB6/SCL_Q4: now also R70.2, U$5.P$24, U$5.P$7, U5.4; no longer R222.2, U21.4
- net PB7/SDA_Q1: now also R107.2, U$1.P$23, U$1.P$8, U9.5; no longer R69.2, U5.5
- net PB7/SDA_Q2: now also R183.2, U$3.P$23, U$3.P$8, U17.5; no longer R145.2, U13.5
- net PB7/SDA_Q3: now also R259.2, U$4.P$23, U$4.P$8, U25.5; no longer R107.2, U9.5
- net PB7/SDA_Q4: now also R69.2, U$5.P$23, U$5.P$8, U5.5; no longer R221.2, U21.5
- net PEN-SCL-FILT_Q1: now also Q15.4, R113.2, R80.1, R84.1, R88.1, TP40.1, U9.15; no longer Q10.4, R42.1, R46.1, R50.1, R75.2, TP25.1, U5.15
- net PEN-SCL-FILT_Q2: now also Q25.4, R156.1, R160.1, R164.1, R189.2, TP70.1, U17.15; no longer Q20.4, R118.1, R122.1, R126.1, R151.2, TP55.1, U13.15
- net PEN-SCL-FILT_Q3: now also Q35.4, R232.1, R236.1, R240.1, R265.2, TP100.1, U25.15; no longer Q15.4, R113.2, R80.1, R84.1, R88.1, TP40.1, U9.15
- net PEN-SCL-FILT_Q4: now also Q10.4, R42.1, R46.1, R50.1, R75.2, TP25.1, U5.15; no longer Q30.4, R194.1, R198.1, R202.1, R227.2, TP85.1, U21.15
- net PEN-SDA-FILT_Q1: now also Q15.6, R109.2, R82.2, R86.2, R90.2, TP41.1, U9.16; no longer Q10.6, R44.2, R48.2, R52.2, R71.2, TP26.1, U5.16
- net PEN-SDA-FILT_Q2: now also Q25.6, R158.2, R162.2, R166.2, R185.2, TP71.1, U17.16; no longer Q20.6, R120.2, R124.2, R128.2, R147.2, TP56.1, U13.16
- net PEN-SDA-FILT_Q3: now also Q35.6, R234.2, R238.2, R242.2, R261.2, TP101.1, U25.16; no longer Q15.6, R109.2, R82.2, R86.2, R90.2, TP41.1, U9.16
- net PEN-SDA-FILT_Q4: now also Q10.6, R44.2, R48.2, R52.2, R71.2, TP26.1, U5.16; no longer Q30.6, R196.2, R200.2, R204.2, R223.2, TP86.1, U21.16
- net POUT_Q1: now also TP31.1, U10.13; no longer TP2.1, U6.13
- net POUT_Q2: now also TP61.1, U18.13; no longer TP46.1, U14.13
- net POUT_Q3: now also TP91.1, U26.13; no longer TP31.1, U10.13
- net POUT_Q4: now also TP2.1, U6.13; no longer TP76.1, U22.13
- net VBUS: now also Q22.4, Q32.4, R169.2, R245.2; no longer Q17.4, Q27.4, R131.2, R207.2
- net VBUSP_Q1: now also C12.2, Q11.1, Q11.2, Q11.5, Q11.6, R77.2, TP37.1, U$1.P$12, U$1.P$13, U$1.P$18, U$1.P$19, U$1.P$27, U$1.P$28, U$1.P$3, U$1.P$4; no longer C7.2, Q6.1, Q6.2, Q6.5, Q6.6, R39.2, TP21.1
- net VBUSP_Q2: now also C22.2, Q21.1, Q21.2, Q21.5, Q21.6, R153.2, TP67.1, U$3.P$12, U$3.P$13, U$3.P$18, U$3.P$19, U$3.P$27, U$3.P$28, U$3.P$3, U$3.P$4; no longer C17.2, Q16.1, Q16.2, Q16.5, Q16.6, R115.2, TP52.1
- net VBUSP_Q3: now also C32.2, Q31.1, Q31.2, Q31.5, Q31.6, R229.2, TP97.1, U$4.P$12, U$4.P$13, U$4.P$18, U$4.P$19, U$4.P$27, U$4.P$28, U$4.P$3, U$4.P$4; no longer C12.2, Q11.1, Q11.2, Q11.5, Q11.6, R77.2, TP37.1
- net VBUSP_Q4: now also C7.2, Q6.1, Q6.2, Q6.5, Q6.6, R39.2, TP21.1, U$5.P$12, U$5.P$13, U$5.P$18, U$5.P$19, U$5.P$27, U$5.P$28, U$5.P$3, U$5.P$4; no longer C27.2, Q26.1, Q26.2, Q26.5, Q26.6, R191.2, TP82.1
- net VPD_Q1: now also C11.2, R104.2, R110.2, R114.2, R78.2, R79.2, R83.2, R87.2, R92.2, TP38.1, U11.5, U12.5, U9.14; no longer C6.2, R40.2, R41.2, R45.2, R49.2, R54.2, R66.2, R72.2, R76.2, TP23.1, U5.14, U7.5, U8.5
- net VPD_Q2: now also C21.2, R154.2, R155.2, R159.2, R163.2, R168.2, R180.2, R186.2, R190.2, TP68.1, U17.14, U19.5, U20.5; no longer C16.2, R116.2, R117.2, R121.2, R125.2, R130.2, R142.2, R148.2, R152.2, TP53.1, U13.14, U15.5, U16.5
- net VPD_Q3: now also C31.2, R230.2, R231.2, R235.2, R239.2, R244.2, R256.2, R262.2, R266.2, TP98.1, U25.14, U27.5, U28.5; no longer C11.2, R104.2, R110.2, R114.2, R78.2, R79.2, R83.2, R87.2, R92.2, TP38.1, U11.5, U12.5, U9.14
- net VPD_Q4: now also C6.2, R40.2, R41.2, R45.2, R49.2, R54.2, R66.2, R72.2, R76.2, TP23.1, U5.14, U7.5, U8.5; no longer C26.2, R192.2, R193.2, R197.2, R201.2, R206.2, R218.2, R224.2, R228.2, TP83.1, U21.14, U23.5, U24.5
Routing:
- net OPD_SDA: track 14.0 -> 29.1 mm
- net VPD_Q2: track 0.00 -> 9.11 mm, vias 0 -> 1
- net N$217: track 0.00 -> 7.84 mm
- net OPD_PWR: track 18.2 -> 11.0 mm
- net N$220: track 0.00 -> 5.99 mm
- net OPD_SCL: track 15.7 -> 12.1 mm
- net GND: track 2.54 -> 5.77 mm, vias 1 -> 3
- net N$222: track 0.00 -> 3.22 mm
- net PEN-SDA-FILT_Q2: track 0.00 -> 1.93 mm
- net N$219: track 0.00 -> 1.63 mm
- net N$216: track 0.00 -> 1.22 mm
